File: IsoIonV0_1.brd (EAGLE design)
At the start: 41.9 x 27.9 mm, 56 parts, among them IC1 MCP3221, IC2 MCP4017-100K, IC4 TL072, IC5 TPS60400DBV

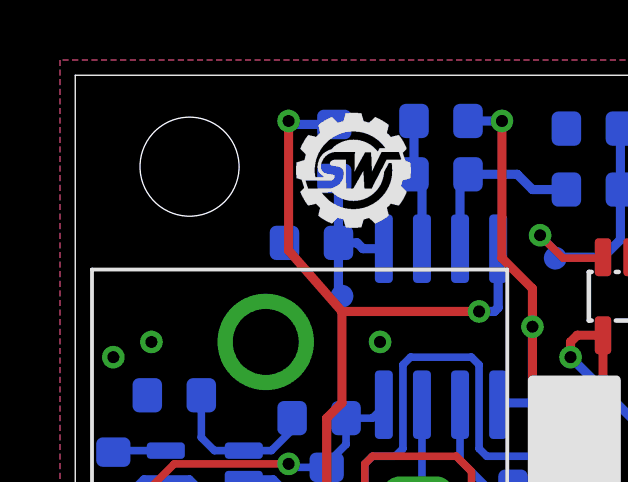
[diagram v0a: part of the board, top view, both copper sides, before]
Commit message: Standoff position fixed, was incorrectly offset
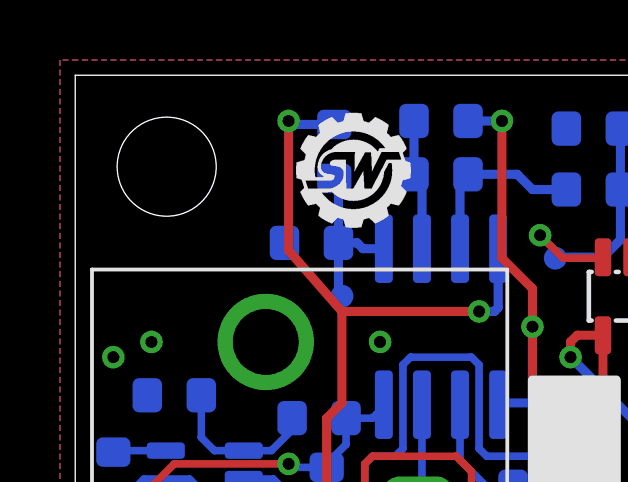
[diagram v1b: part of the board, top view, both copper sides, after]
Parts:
- moved JP4 0.76 mm to (3.05, 24.9)
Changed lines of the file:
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@@
 <element name="JP2" library="SparkFun" package="STAND-OFF" value="STAND-OFF" x="3.048" y="3.048"/>
 <element name="JP3" library="SparkFun" package="STAND-OFF" value="STAND-OFF" x="38.862" y="24.892"/>
-<element name="JP4" library="SparkFun" package="STAND-OFF" value="STAND-OFF" x="3.81" y="24.892"/>
+<element name="JP4" library="SparkFun" package="STAND-OFF" value="STAND-OFF" x="3.048" y="24.892"/>
 <element name="J1" library="Connector" package="4P-2.0" value="" x="28.448" y="4.572" smashed="yes">
 <attribute name="NAME" x="26.823" y="5.372" size="0.8128" layer="33" font="vector" ratio="10"/>
